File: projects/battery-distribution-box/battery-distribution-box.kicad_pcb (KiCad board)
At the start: 2 copper layers, 60 x 65 mm, 10 parts, among them J1 Cells, J2 Diag, J3 Balancer, J4 Output, J5 Balancer enable

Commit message: Project was overnested.
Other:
- board text added: "Battery distribution box v1.0.0 Copyright (c) 2026 devbotas"
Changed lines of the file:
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@@
 			(outputformat 1)
 			(mirror no)
-			(drillshape 1)
+			(drillshape 0)
 			(scaleselection 1)
-			(outputdirectory "")
+			(outputdirectory "output")
 		)
 	)
@@
 		)
 	)
+	(gr_text "Battery distribution box v1.0.0\nCopyright (c) 2026 devbotas"
+		(at 107 118 90)
+		(layer "F.SilkS")
+		(effects
+			(font
+				(size 1.5 1.5)
+				(thickness 0.3)
+				(bold yes)
+			)
+			(justify bottom)
+		)
+	)

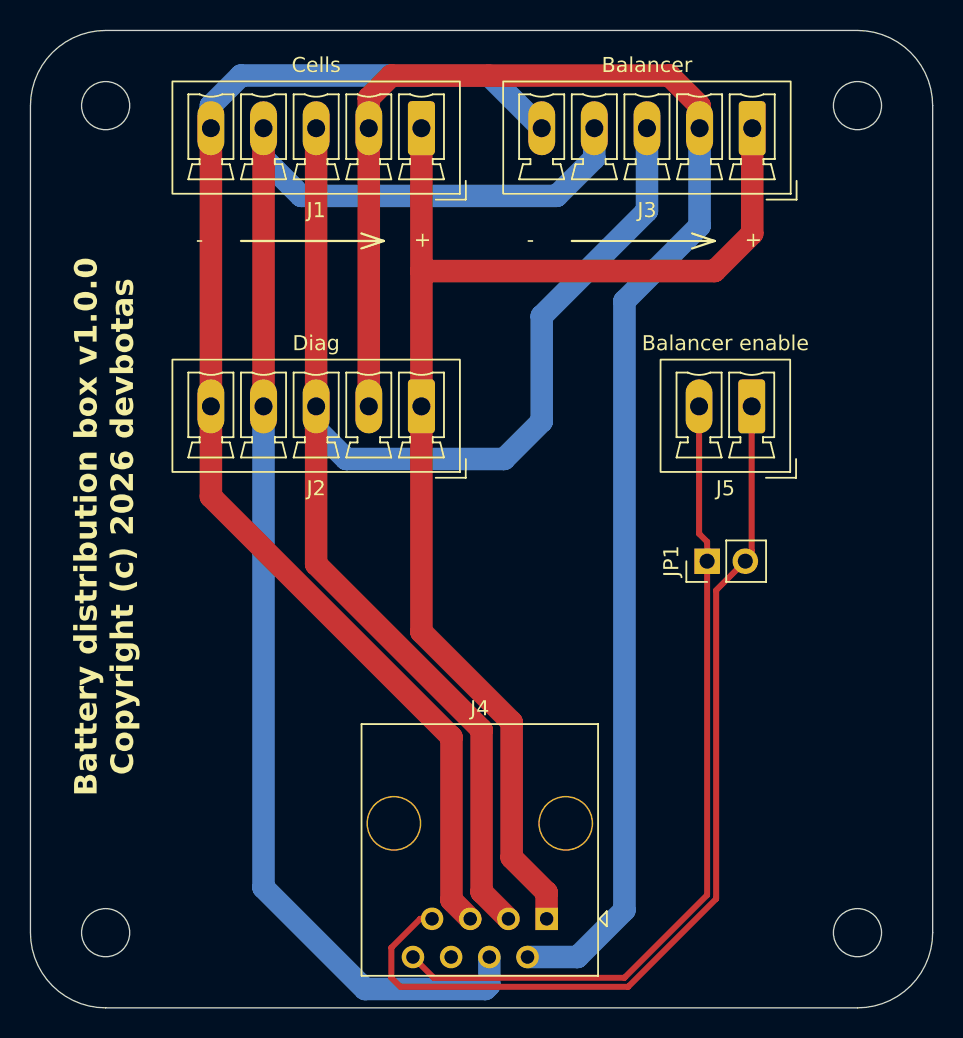
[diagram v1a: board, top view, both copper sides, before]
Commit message: Moving to JST VH connectors. They are cheaper and easier to source.
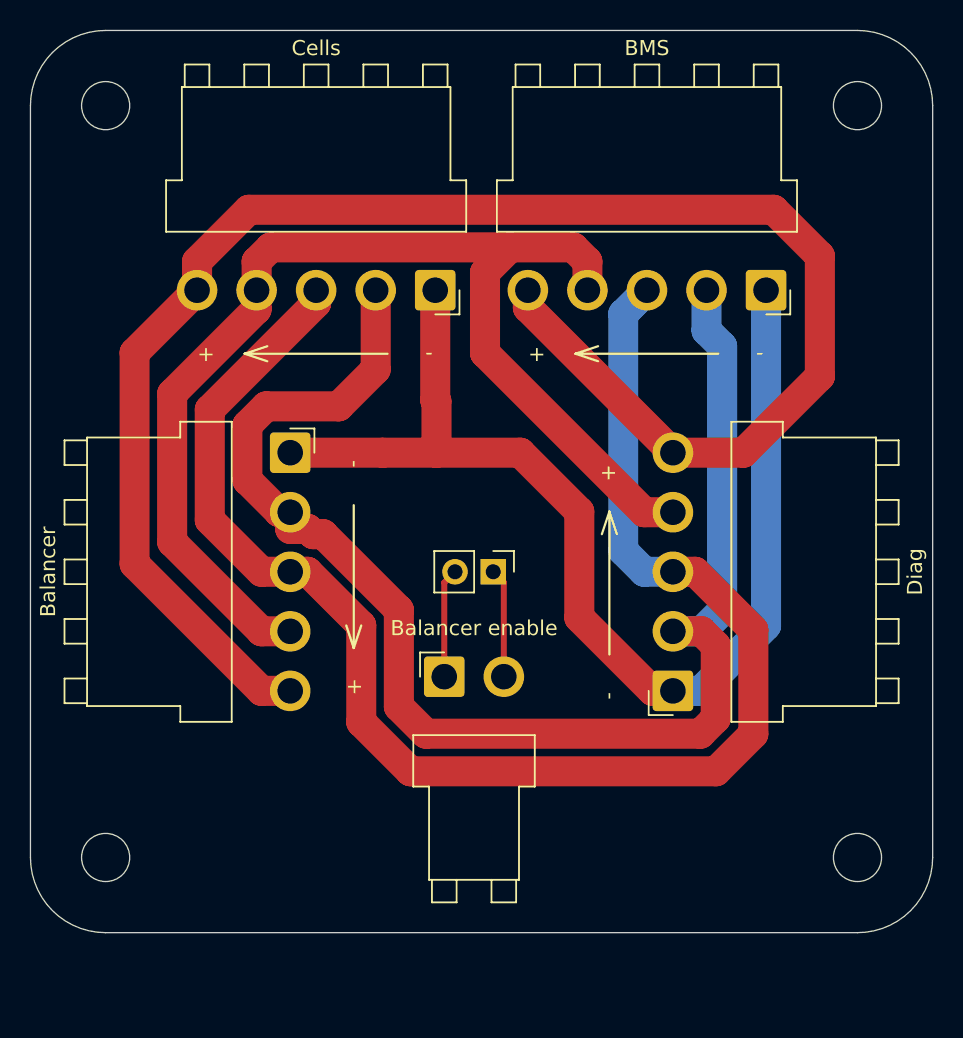
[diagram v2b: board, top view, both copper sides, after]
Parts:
- removed J4: Output, Connector_RJ:RJ45_OST_PJ012-8P8CX_Vertical
- added J6: Diag, Connector_JST:JST_VH_B5PS-VH_1x05_P3.96mm_Horizontal, F.Cu at (142.7, 128.9)
- J1: footprint Connector_Phoenix_MC:PhoenixContact_MCV_1,5_5-G-3.5_1x05_P3.50mm_Vertical -> Connector_JST:JST_VH_B5PS-VH_1x05_P3.96mm_Horizontal
- J2: value Diag -> Balancer; footprint Connector_Phoenix_MC:PhoenixContact_MCV_1,5_5-G-3.5_1x05_P3.50mm_Vertical -> Connector_JST:JST_VH_B5PS-VH_1x05_P3.96mm_Horizontal
- J3: value Balancer -> BMS; footprint Connector_Phoenix_MC:PhoenixContact_MCV_1,5_5-G-3.5_1x05_P3.50mm_Vertical -> Connector_JST:JST_VH_B5PS-VH_1x05_P3.96mm_Horizontal
- J5: footprint Connector_Phoenix_MC:PhoenixContact_MCV_1,5_2-G-3.5_1x02_P3.50mm_Vertical -> Connector_JST:JST_VH_B2PS-VH_1x02_P3.96mm_Horizontal
- moved J5 27.2 mm to (127.5, 128.0), turned to 0 degrees
- moved JP1 14.2 mm to (130.8, 121.0), turned to -90 degrees
- moved J1 10.8 mm to (126.9, 102.3)
- moved J3 10.8 mm to (148.9, 102.3)
- moved J2 9.25 mm to (117.3, 113.1), turned to -90 degrees
- moved REF** 5.00 mm to (105.0, 140.0)
- moved REF** 5.00 mm to (155.0, 140.0)
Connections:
- net Net-(J1-Pin_1) renamed /B0
- net Net-(J1-Pin_2) renamed /B1
- net Net-(J1-Pin_3) renamed /B2
- net Net-(J1-Pin_4) renamed /B3
- net Net-(J1-Pin_5) renamed /B4
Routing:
- net Net-(J5-Pin_1): track 63.5 -> 7.27 mm
- net Net-(J5-Pin_2): track 55.1 -> 7.27 mm
- net /B4: track 85.5 -> 114.5 mm
- net /B3: track 98.4 -> 80.6 mm
- net /B1: track 107.3 -> 95.7 mm
- net /B0: track 86.1 -> 77.3 mm
- net /B2: track 98.6 -> 101.8 mm
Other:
- board size 60 x 65 mm -> 60 x 60 mm
- board text added: "Battery distribution box v2.0.0 Copyright (c) 2026 devbotas"
- board text removed: "Battery distribution box v1.0.0 Copyright (c) 2026 devbotas"
